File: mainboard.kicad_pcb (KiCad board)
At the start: 4 copper layers, 44.4 x 35.8 mm, 43 parts, among them IC1 BMX160, J1 Conn_01x01, J2 10118194-0001LF, J28 Conn_01x01, J29 Conn_01x01, J3 Micro_SD_Card, J30 Conn_01x01, J4 xf2m-2415-1a, J5 XF2M-1015-1A, SW1 KMR231NG LFS, U1 RFM95W-915S2, U2 ATSAMD51G_TQFN48, U3 DRV8848, U4 TPS82740BSIPR, U5 DRV8848, U6 MAX708RESA-T, U8 RFM95W-915S2, X1 ANTENNA_U.FL

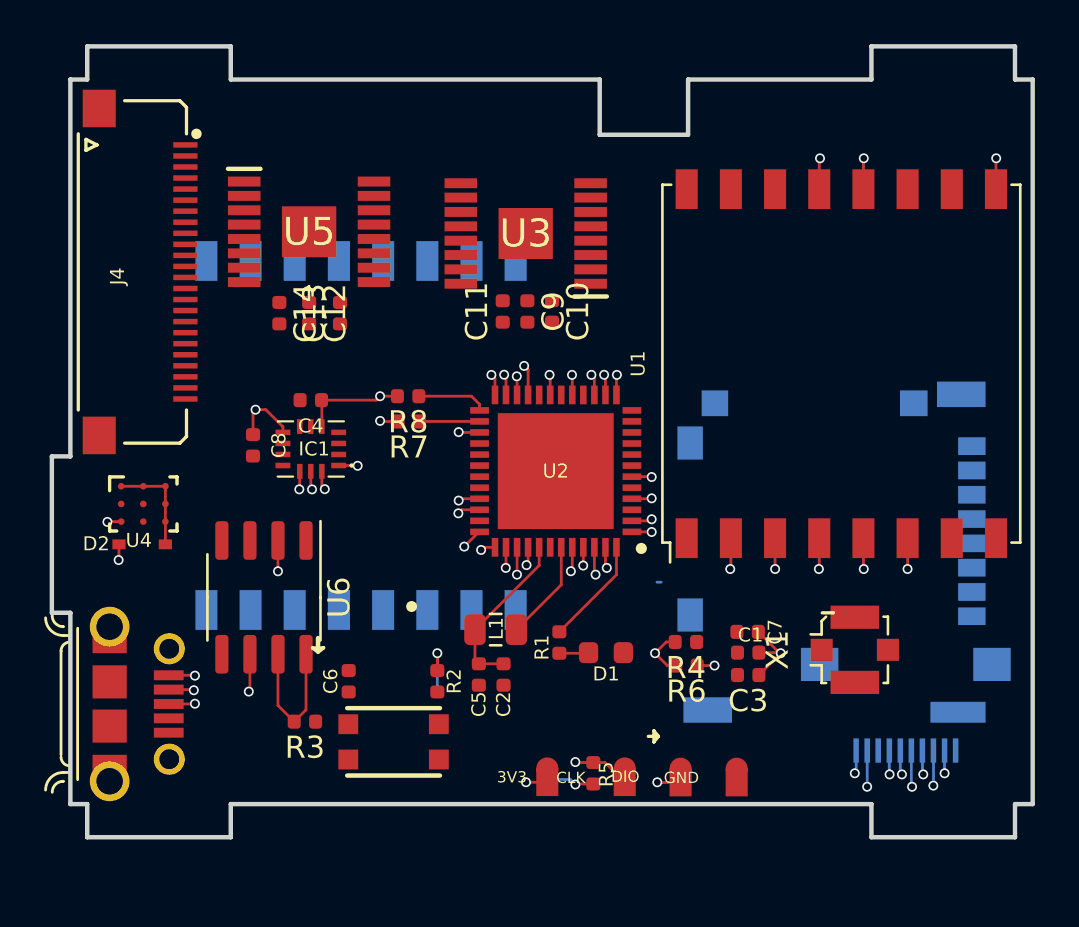
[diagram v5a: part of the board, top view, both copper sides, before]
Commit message: updated camera placement to avoid vertical pulling
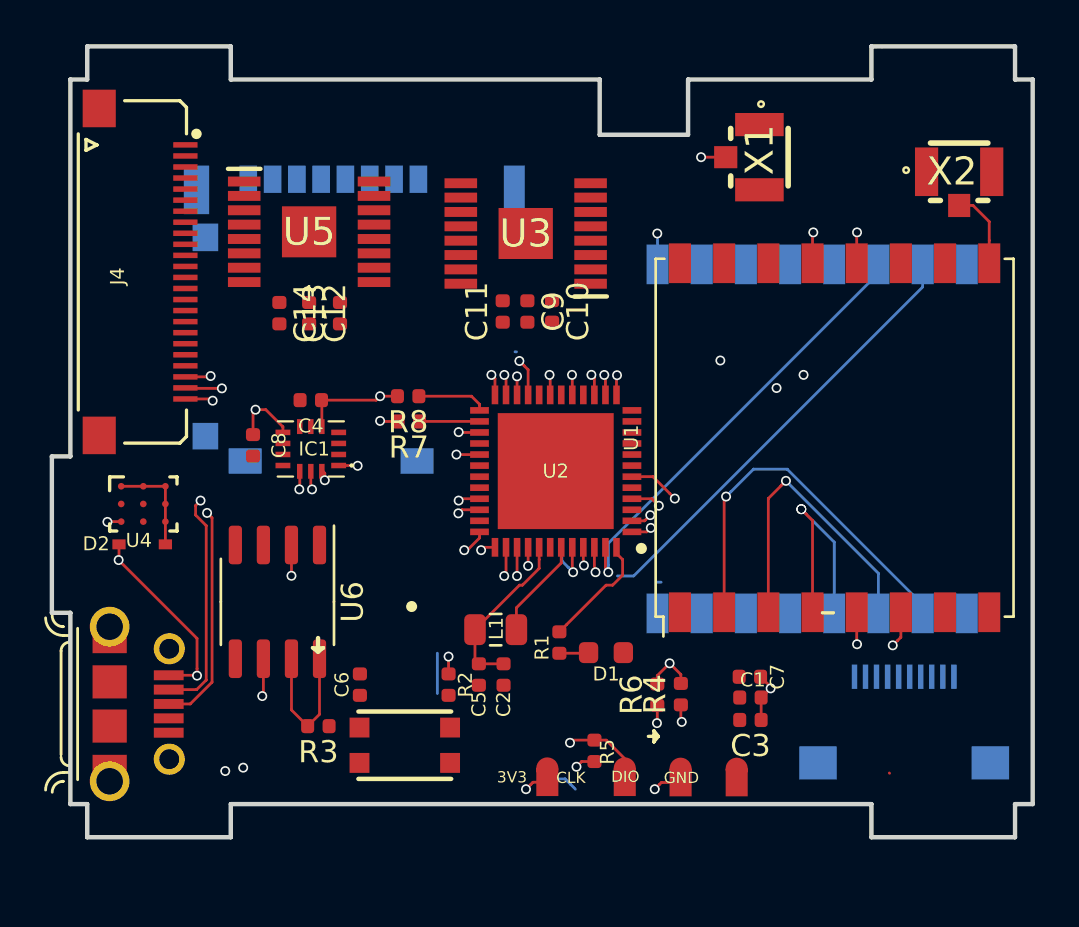
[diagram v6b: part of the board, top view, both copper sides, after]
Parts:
- added X2: ANTENNA_U.FL, U.FL:UFL-R-SMT01, F.Cu at (117.7, 79.3)
- X1: footprint Connector_Coaxial:U.FL_Molex_MCRF_73412-0110_Vertical -> U.FL:UFL-R-SMT01
- moved J3 25.0 mm to (90.3, 85.3), turned to 180 degrees
- moved X1 22.7 mm to (108.7, 78.7)
- moved U8 20.4 mm to (111.0, 91.4)
- moved U1 3.37 mm to (112.1, 91.4)
- moved J5 3.34 mm to (115.2, 102.2), turned to 180 degrees
- moved R4 2.37 mm to (105.1, 103.0), turned to 90 degrees
- moved C3 2.03 mm to (108.3, 104.2)
- moved C1 2.03 mm to (108.3, 103.1)
- moved C7 2.03 mm to (108.2, 102.2)
- moved R6 1.87 mm to (104.0, 103.0), turned to 90 degrees
- moved R5 1.02 mm to (101.2, 105.6)
- moved U6 0.64 mm to (86.8, 98.8)
- moved R3 0.64 mm to (88.7, 104.4)
- moved C6 0.53 mm to (90.6, 102.6)
- moved R2 0.53 mm to (94.6, 102.6)
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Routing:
- net MISO: track 4.33 -> 58.6 mm
- net SCK: track 4.21 -> 57.4 mm, vias 4 -> 5
- net MOSI: track 4.76 -> 56.4 mm
- net BATT_N: track 1.10 -> 48.6 mm, vias 1 -> 2
- net BATT_P: track 1.13 -> 46.8 mm, vias 1 -> 2
- net /USB-: track 2.13 -> 23.0 mm
- net RF_DIO1: track 1.24 -> 21.6 mm
- net /USB+: track 2.22 -> 22.5 mm
- net EN_CAM: track 1.15 -> 21.3 mm
- net RF_DIO0: track 0.96 -> 20.2 mm
- net CS_CAM: track 2.62 -> 20.5 mm, vias 2 -> 1
- net SCL1: track 0.92 -> 11.9 mm, vias 1 -> 2
- net SDA1: track 1.68 -> 10.7 mm
- net VUSB: track 1.91 -> 8.71 mm
- net Net-(U8-Pad9): track 0.00 -> 6.79 mm, vias 0 -> 2
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
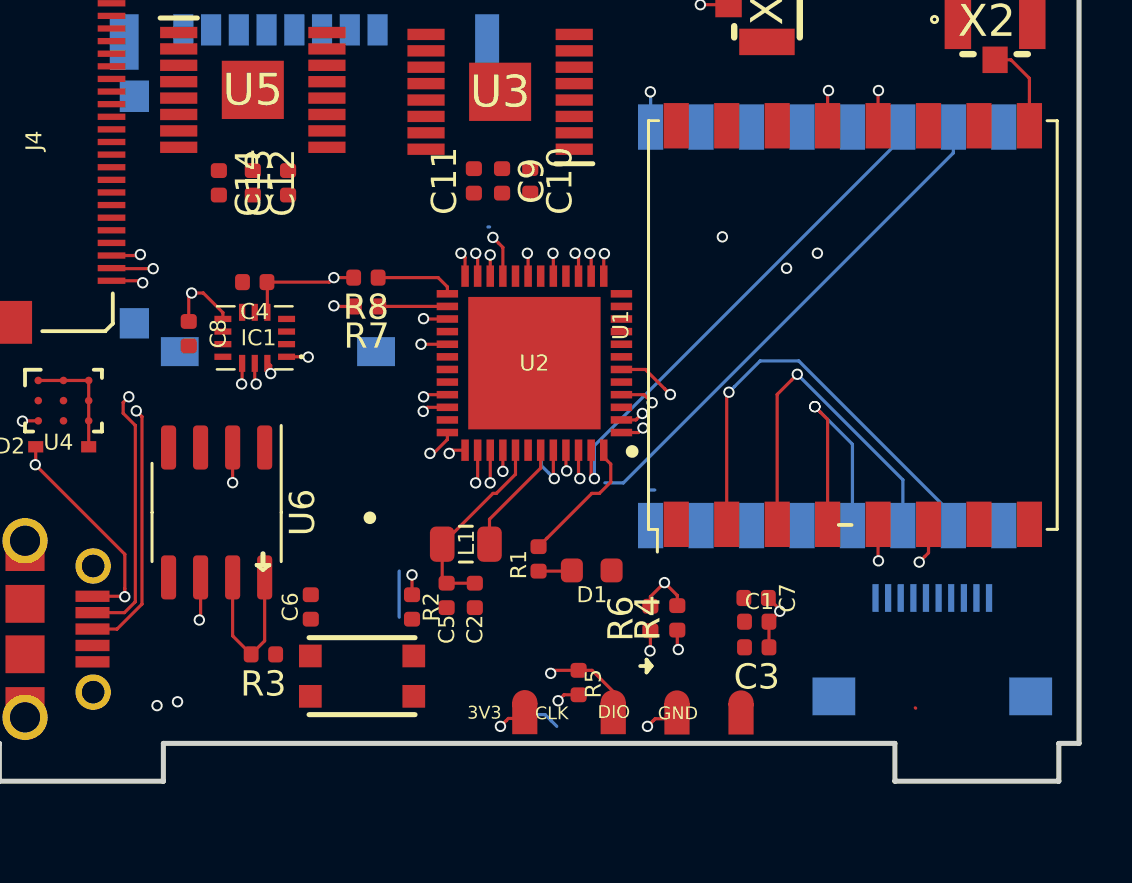
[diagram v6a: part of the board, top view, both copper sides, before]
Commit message: updated traces
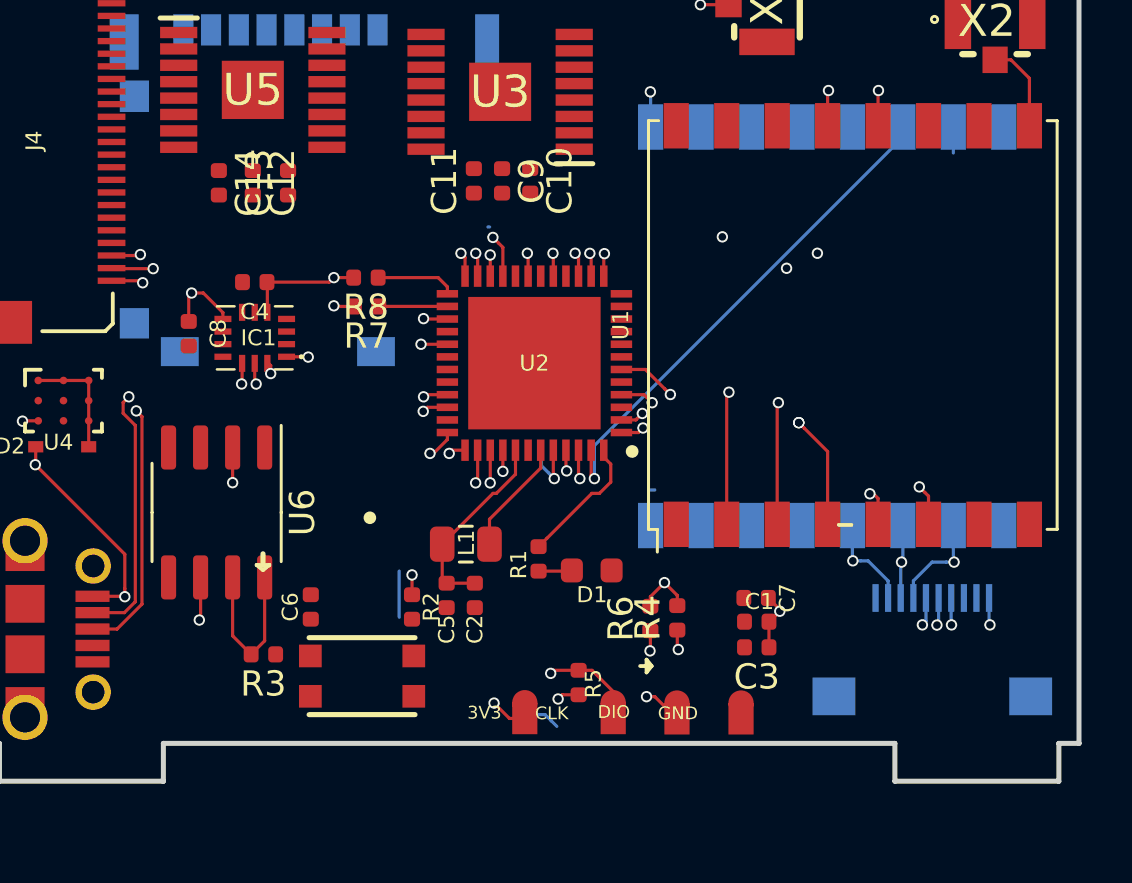
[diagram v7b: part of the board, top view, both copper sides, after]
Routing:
- net BATT_N: track 48.6 -> 2.73 mm
- net BATT_P: track 46.8 -> 2.42 mm
- net RF_DIO1: track 21.6 -> 2.32 mm
- net EN_CAM: track 21.3 -> 2.15 mm, vias 1 -> 2
- net CS_CAM: track 20.5 -> 2.10 mm, vias 1 -> 2
- net MISO: track 58.6 -> 53.2 mm, vias 4 -> 5
- net MOSI: track 56.4 -> 51.8 mm, vias 4 -> 5
- net SCK: track 57.4 -> 55.0 mm, vias 5 -> 6

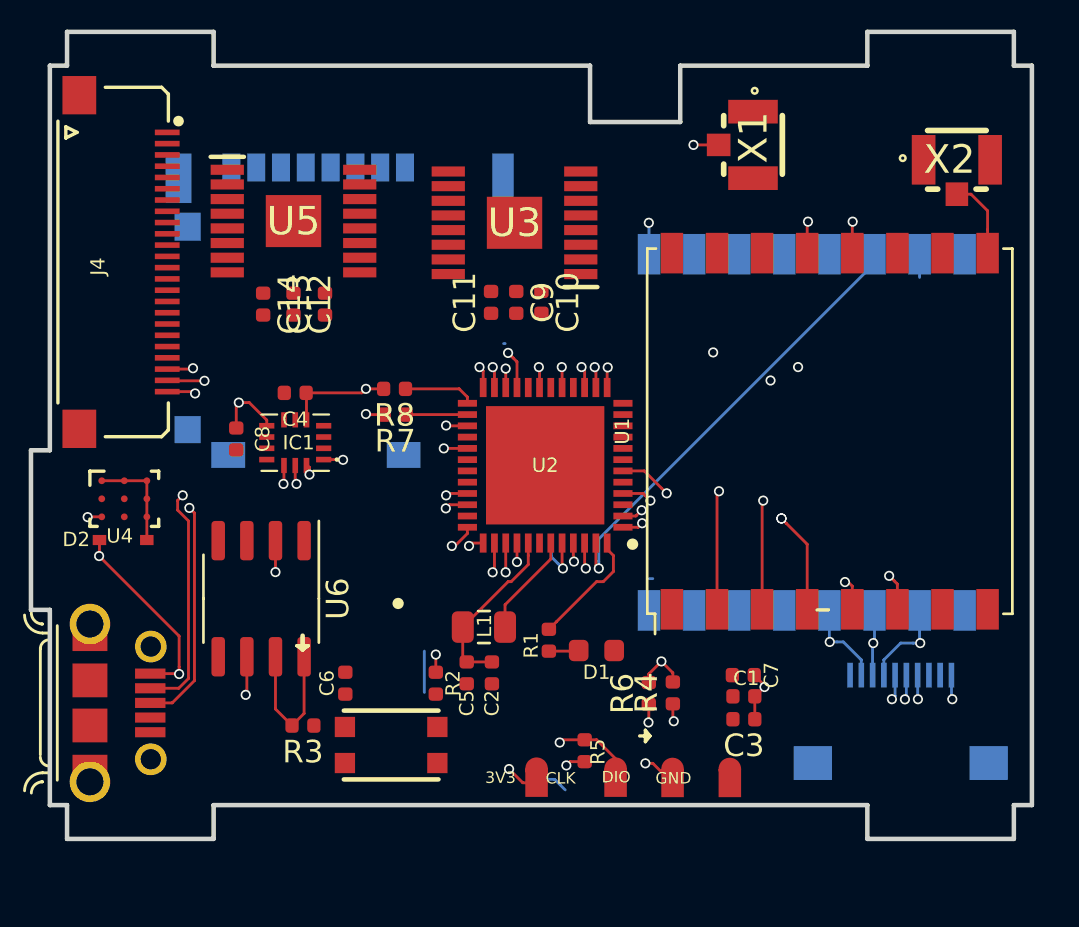
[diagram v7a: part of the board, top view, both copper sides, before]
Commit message: adjusted ordering in flat flex connector to avoid ratsnest crossings for Hbridges, added camera traces
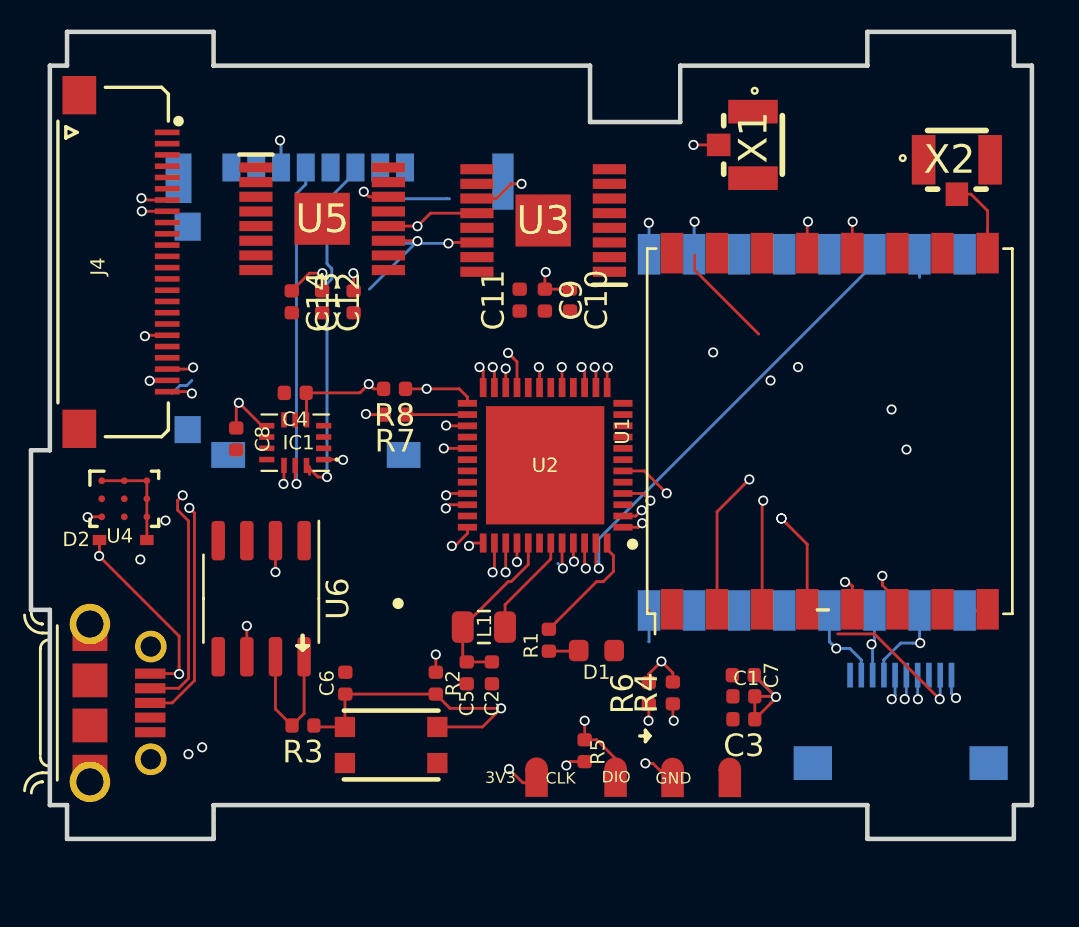
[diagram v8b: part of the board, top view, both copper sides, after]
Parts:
- moved C10 1.27 mm to (100.5, 85.6)
- moved C12 1.27 mm to (89.5, 85.6)
- moved U5 1.27 mm to (89.5, 82.0)
- moved C11 1.27 mm to (98.3, 85.6)
- moved C13 1.27 mm to (90.9, 85.6)
- moved C14 1.27 mm to (88.2, 85.6)
- moved C9 1.27 mm to (99.4, 85.6)
- moved U3 1.27 mm to (99.4, 82.0)
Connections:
- J4 pad 1: SCL2 -> GND
- J4 pad 10: MOZ_2 -> Net-(J4-Pad10)
- J4 pad 12: MOX_2 -> MOZ_1
- J4 pad 13: Net-(J4-Pad13) -> MOZ_2
- J4 pad 14: MOX_1 -> MOX_2
- J4 pad 15: SCL1 -> MOX_1
- J4 pad 16: SDA1 -> Net-(J4-Pad16)
- J4 pad 19: Net-(J4-Pad19) -> SDA1
- J4 pad 2: SDA2 -> Net-(J4-Pad2)
- J4 pad 20: Net-(J4-Pad20) -> SDA2
- J4 pad 21: GND -> Net-(J4-Pad21)
- J4 pad 23: BATT_N -> SCL1
- J4 pad 24: BATT_P -> SCL2
- J4 pad 5: Net-(J4-Pad5) -> MOY_2
- J4 pad 6: MOY_2 -> Net-(J4-Pad6)
- J4 pad 7: Net-(J4-Pad7) -> BATT_P
- J4 pad 8: MOZ_1 -> BATT_N
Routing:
- net BATT_P: track 2.42 -> 97.0 mm, vias 2 -> 6
- net BATT_N: track 2.73 -> 60.2 mm, vias 2 -> 3
- net SDA1: track 10.7 -> 44.7 mm, vias 2 -> 4
- net CS_CAM: track 2.10 -> 34.0 mm, vias 2 -> 3
- net EN_CAM: track 2.15 -> 33.8 mm, vias 2 -> 3
- net SCL1: track 11.9 -> 41.5 mm, vias 2 -> 4
- net ~RESET: track 0.96 -> 20.9 mm, vias 1 -> 2
- net +3V3: track 32.4 -> 49.4 mm, vias 16 -> 21
- net GND: track 0.00 -> 16.7 mm, vias 0 -> 3
- net SCK: track 55.0 -> 69.8 mm
- net MOSI: track 51.8 -> 66.6 mm
- net SCL2: track 3.17 -> 14.8 mm, vias 0 -> 2
- net WDT_WDI: track 2.39 -> 13.4 mm
- net /SWDIO: track 2.72 -> 12.5 mm
- net /SWCLK: track 3.78 -> 10.7 mm
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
